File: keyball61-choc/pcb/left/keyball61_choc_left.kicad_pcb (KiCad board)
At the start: 2 copper layers, 141.9 x 107.5 mm, 141 parts, among them J1 OLED, J13 TRS_JACK, J2 Conn_01x01-Connector_Generic, J3 Conn_01x01-Connector_Generic, P1 I2C, P2 I2C, SW1 Choc_V1, SW10 Choc_V1, SW11 Choc_V1, SW12 Choc_V1, SW13 Choc_V1, SW14 Choc_V1, SW15 Choc_V1, SW16 Choc_V1, SW17 Choc_V1, SW18 Choc_V1, SW19 Choc_V1, SW2 Choc_V1, SW20 Choc_V1, SW21 Choc_V1, SW22 Choc_V1, SW23 Choc_V1, SW24 Choc_V1, SW25 Choc_V1, SW26 Choc_V1, SW27 Choc_V1, SW28 Choc_V1, SW29 Choc_V1, SW3 Choc_V1, SW30 Choc_V1, SW31 Choc_V1, SW32 Choc_V1, SW33 RESET_SW, SW4 Choc_V1, SW5 Choc_V1, SW6 Choc_V1, SW7 Choc_V1, SW8 Choc_V1, SW9 Choc_V1, U1 ProMicro-kbd

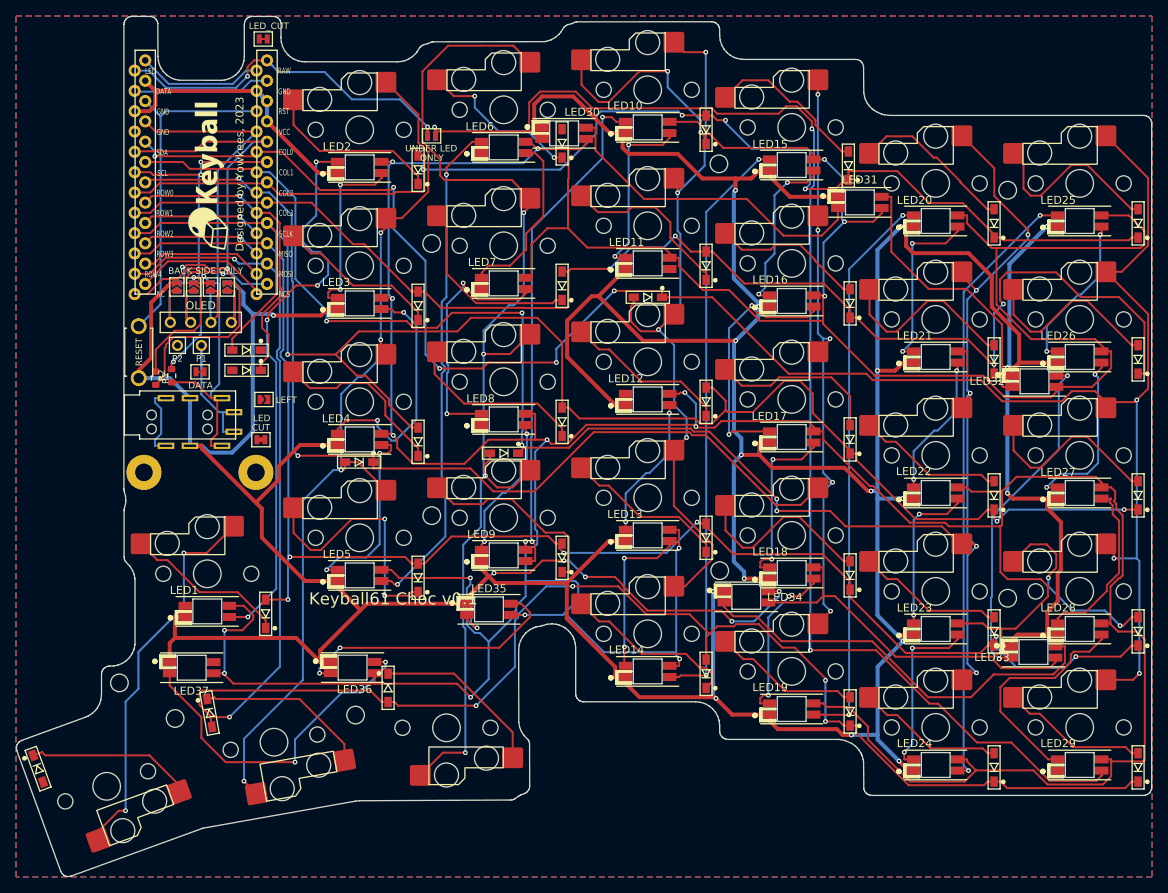
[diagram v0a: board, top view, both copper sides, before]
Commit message: WIP: routed left/right boards from previous run (DRC: L 10 err/7 open, R 9 err/11 open)
Superseded by the routing run in progress.

Co-Authored-By: Claude Opus 5.5 <noreply@anthropic.com>
Claude-Session: https://claude.ai/code/session_012Lz4SD3XgX9T3cBqnotnnt
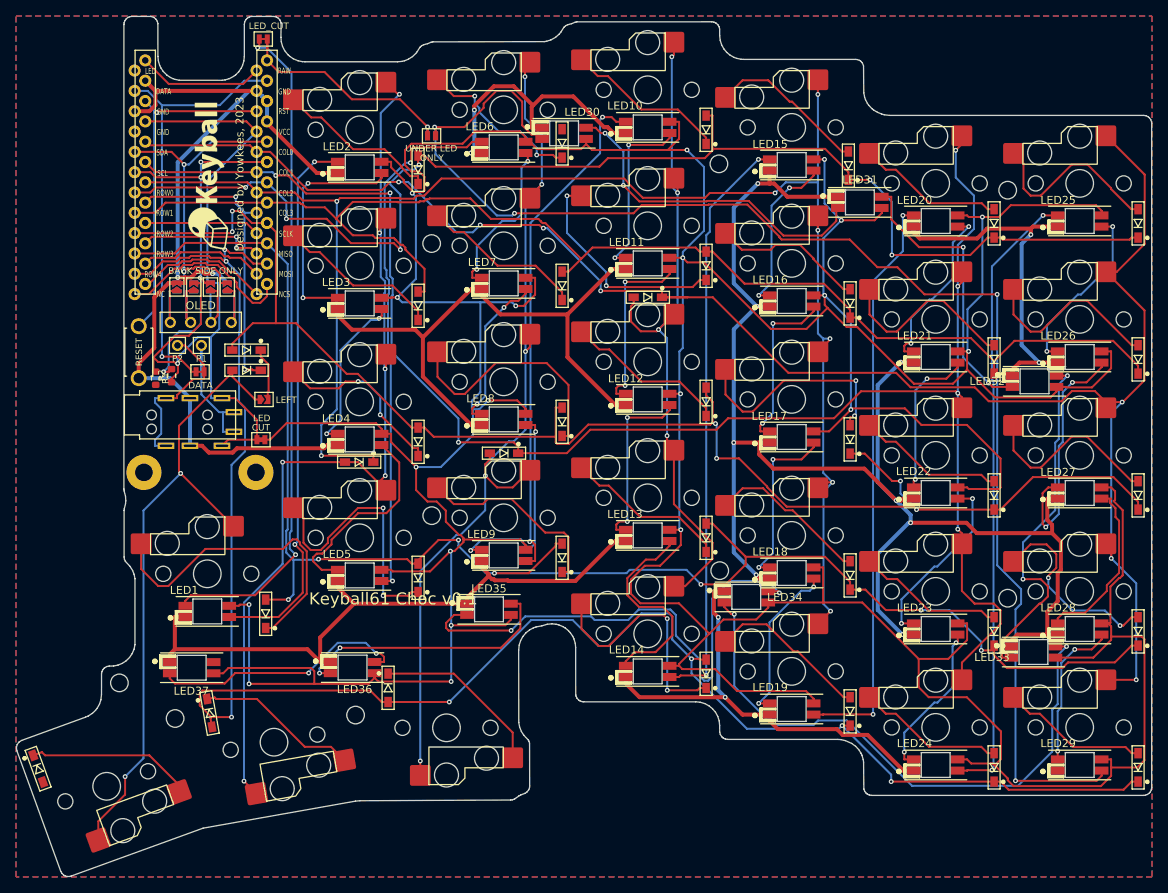
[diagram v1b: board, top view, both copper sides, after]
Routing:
- net Net-(JP12-Pad2): track 0.00 -> 84.9 mm, vias 0 -> 2
- net GND: track 659.0 -> 597.9 mm, vias 18 -> 16
- net DATA: track 17.1 -> 55.2 mm, vias 0 -> 1
- net Net-(JP11-Pad1): track 739.3 -> 706.3 mm, vias 18 -> 20
- net Net-(D37-Pad2): track 48.4 -> 80.5 mm
- net SDA: track 69.4 -> 41.4 mm, vias 2 -> 3
- net Net-(D35-Pad2): track 139.5 -> 112.5 mm, vias 4 -> 5
- net Net-(LED11-Pad2): track 0.00 -> 22.7 mm, vias 0 -> 2
- net Net-(LED33-Pad2): track 53.1 -> 73.9 mm, vias 0 -> 2
- net Net-(D26-Pad1): track 21.0 -> 40.1 mm
- net ROW2: track 206.8 -> 188.6 mm, vias 3 -> 6
- net COL0: track 245.5 -> 227.2 mm, vias 8 -> 7
- net LED: track 46.9 -> 30.3 mm, vias 2 -> 1
- net COL1: track 228.7 -> 214.1 mm, vias 10 -> 7
- net ROW3: track 190.5 -> 204.7 mm, vias 6 -> 7
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
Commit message: WIP: routed boards from previous run (DRC: L 4 err/3 open, R 10 err/8 open)
Superseded by the routing run in progress.

Co-Authored-By: Claude Opus 5.5 <noreply@anthropic.com>
Claude-Session: https://claude.ai/code/session_012Lz4SD3XgX9T3cBqnotnnt
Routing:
- net GND: track 597.9 -> 743.0 mm, vias 16 -> 10
- net Net-(JP11-Pad1): track 706.3 -> 774.6 mm, vias 20 -> 17
- net COL0: track 227.2 -> 161.1 mm, vias 7 -> 3
- net SDA: track 41.4 -> 63.4 mm, vias 3 -> 4
- net LED: track 30.3 -> 50.3 mm, vias 1 -> 2
- net Net-(LED33-Pad2): track 73.9 -> 56.1 mm, vias 2 -> 4
- net ROW2: track 188.6 -> 171.0 mm
- net Net-(LED27-Pad2): track 22.1 -> 39.4 mm
- net COL2: track 205.9 -> 222.3 mm, vias 8 -> 7
- net Net-(D26-Pad1): track 40.1 -> 26.1 mm, vias 0 -> 2
- net Net-(D25-Pad1): track 33.3 -> 20.5 mm, vias 2 -> 0
- net Net-(D4-Pad1): track 20.4 -> 30.9 mm
- net Net-(LED26-Pad2): track 31.1 -> 20.7 mm
- net Net-(D17-Pad1): track 30.3 -> 20.4 mm, vias 0 -> 2
- net Net-(LED31-Pad2): track 35.9 -> 45.5 mm
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
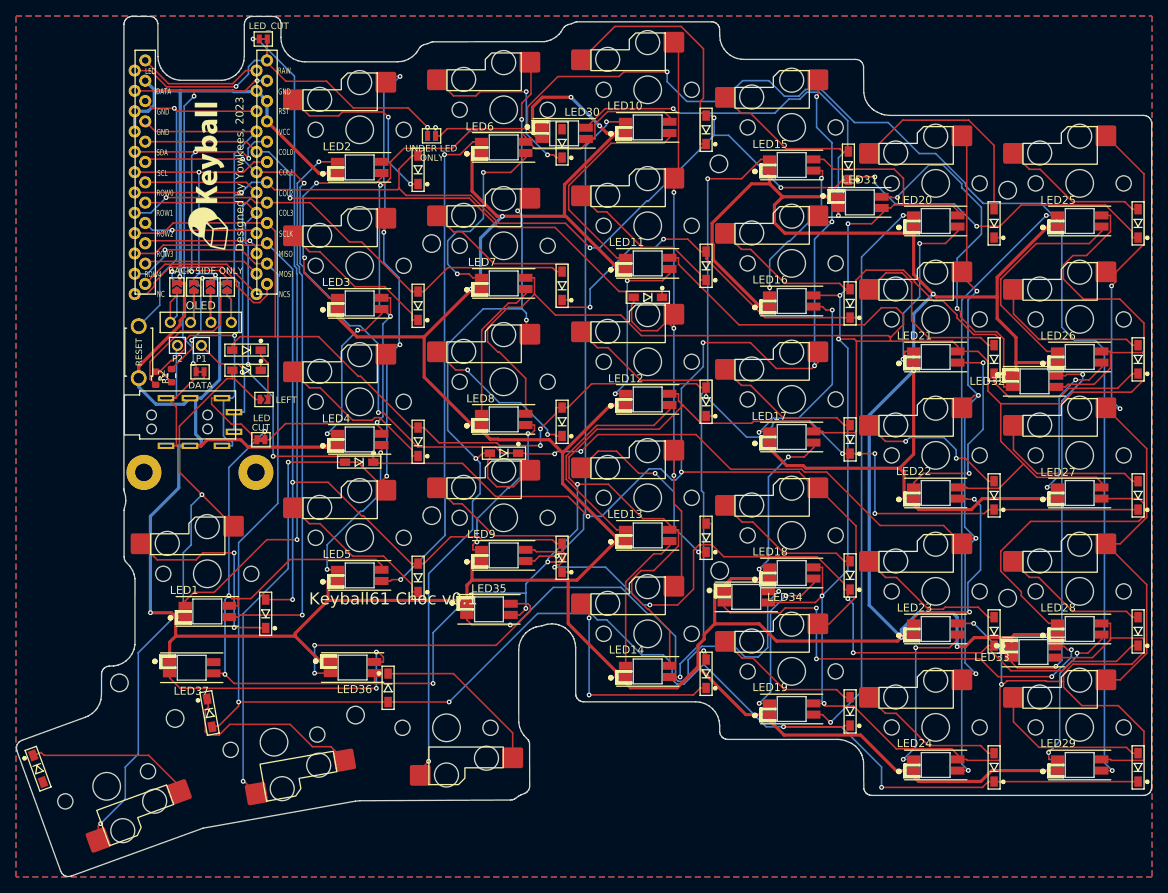
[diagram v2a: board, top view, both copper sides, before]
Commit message: WIP: boards from previous routing run (DRC: L 14 err/2 open, R 28 err/6 open)
Superseded by the iterative routing run in progress.

Co-Authored-By: Claude Opus 5.5 <noreply@anthropic.com>
Claude-Session: https://claude.ai/code/session_012Lz4SD3XgX9T3cBqnotnnt
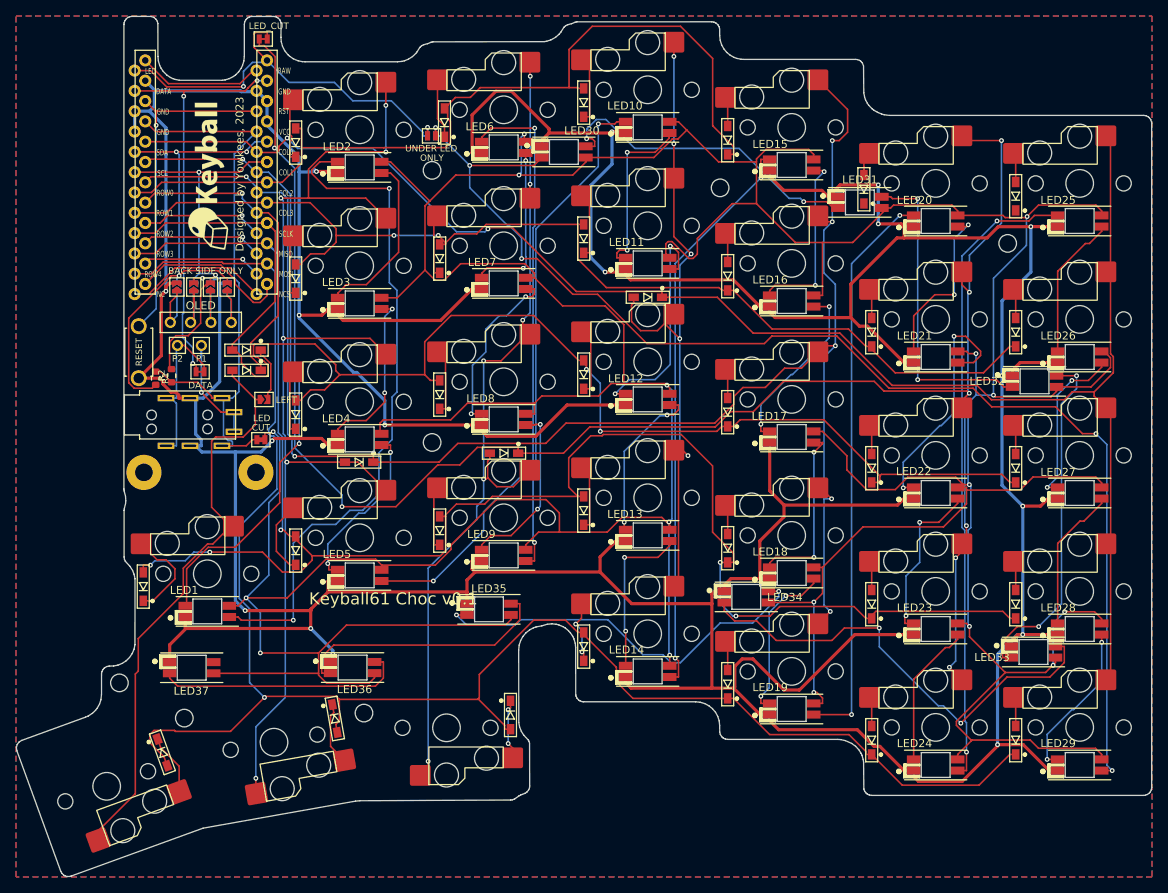
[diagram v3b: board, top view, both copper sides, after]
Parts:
- removed MH5, MH7: M2, keyball61_choc:MountingHole_2.2mm_M2
- moved D2 16.8 mm to (186.1, 64.1)
- moved D27 15.7 mm to (205.1, 133.0)
- moved D28 15.7 mm to (187.1, 133.0)
- moved D20 15.7 mm to (205.1, 116.0)
- moved D21 15.7 mm to (187.1, 116.0)
- moved D22 15.7 mm to (169.1, 109.0)
- moved D23 15.7 mm to (151.1, 104.3)
- moved D24 15.7 mm to (133.1, 106.8)
- moved D30 15.7 mm to (151.1, 121.3)
- moved D31 15.7 mm to (142.0, 129.8)
- moved D4 15.7 mm to (151.1, 53.3)
- moved D1 15.7 mm to (205.1, 65.0)
- moved D10 15.7 mm to (151.1, 70.3)
- moved D11 15.7 mm to (133.1, 72.8)
- moved D13 15.7 mm to (205.1, 99.0)
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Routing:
- net Net-(JP11-Pad1): track 774.6 -> 688.2 mm
- net ROW0: track 156.4 -> 109.0 mm, vias 6 -> 0
- net COL0: track 161.1 -> 206.9 mm, vias 3 -> 2
- net ROW1: track 165.0 -> 135.0 mm, vias 3 -> 2
- net Net-(D36-Pad2): track 118.2 -> 141.0 mm
- net Net-(D4-Pad1): track 30.9 -> 8.27 mm
- net Net-(D2-Pad2): track 26.6 -> 4.01 mm
- net Net-(LED27-Pad2): track 39.4 -> 18.2 mm
- net Net-(D8-Pad2): track 23.0 -> 3.69 mm
- net Net-(D30-Pad1): track 26.8 -> 7.84 mm
- net Net-(D13-Pad2): track 20.3 -> 3.69 mm
- net Net-(D7-Pad2): track 20.3 -> 3.69 mm
- net Net-(D27-Pad2): track 20.3 -> 3.69 mm
- net COL2: track 222.3 -> 206.3 mm
- net Net-(D23-Pad1): track 24.2 -> 8.27 mm, vias 2 -> 0
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
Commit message: Iteratively routed boards (0 DRC violations; L 2 / R 7 open) + fixup.py grid router with rip-up
Co-Authored-By: Claude Opus 5.5 <noreply@anthropic.com>
Claude-Session: https://claude.ai/code/session_012Lz4SD3XgX9T3cBqnotnnt
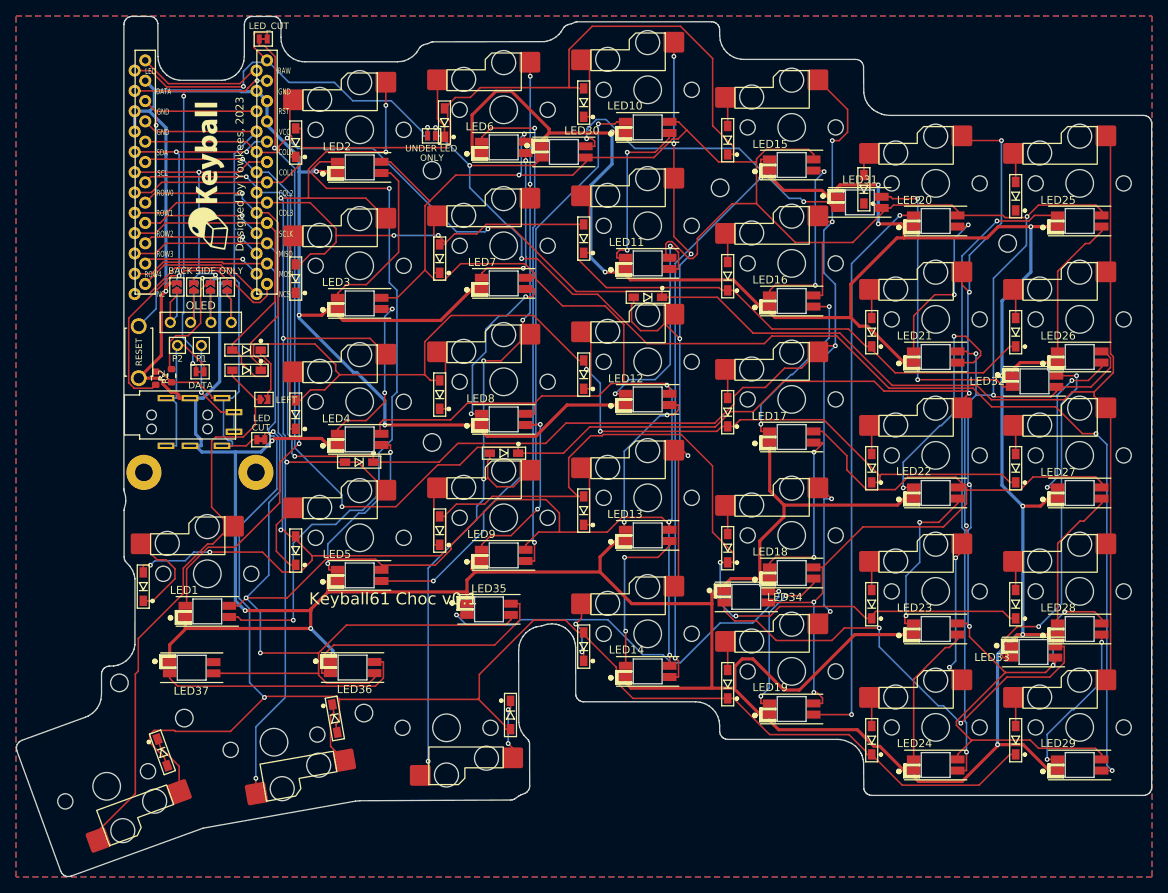
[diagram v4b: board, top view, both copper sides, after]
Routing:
- net Net-(J1-Pad2): track 10.0 -> 8.24 mm
- net Net-(J13-PadA): track 14.8 -> 13.4 mm
- net GND: track 745.7 -> 744.7 mm
- net Net-(D2-Pad2): track 4.01 -> 3.00 mm
- net ROW3: track 211.5 -> 210.5 mm
- net LED: track 54.0 -> 53.2 mm
- net ROW2: track 175.4 -> 174.7 mm
- net Net-(U1-Pad12): track 22.5 -> 21.8 mm
- net ROW4: track 219.5 -> 219.0 mm
- net Net-(D32-Pad1): track 8.41 -> 7.87 mm
- net Net-(JP12-Pad2): track 81.8 -> 81.3 mm
- net Net-(JP13-Pad1): track 158.2 -> 157.7 mm
- net Net-(LED33-Pad2): track 58.8 -> 58.3 mm
- net Net-(J13-PadB): track 21.2 -> 20.7 mm

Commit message: Keyball61 Choc v0.1: DRC-clean routed PCBs, JLC fab files, bottom plates, renders
Both halves: 0 DRC errors, 0 unconnected (KiCad 9). Gerbers + drill,
JLC BOM/CPL (single-sided assembly), 2 mm acrylic bottom plates with the
original trackball-case holes, and 3D renders. Docs updated.

Co-Authored-By: Claude Opus 5.5 <noreply@anthropic.com>
Claude-Session: https://claude.ai/code/session_012Lz4SD3XgX9T3cBqnotnnt
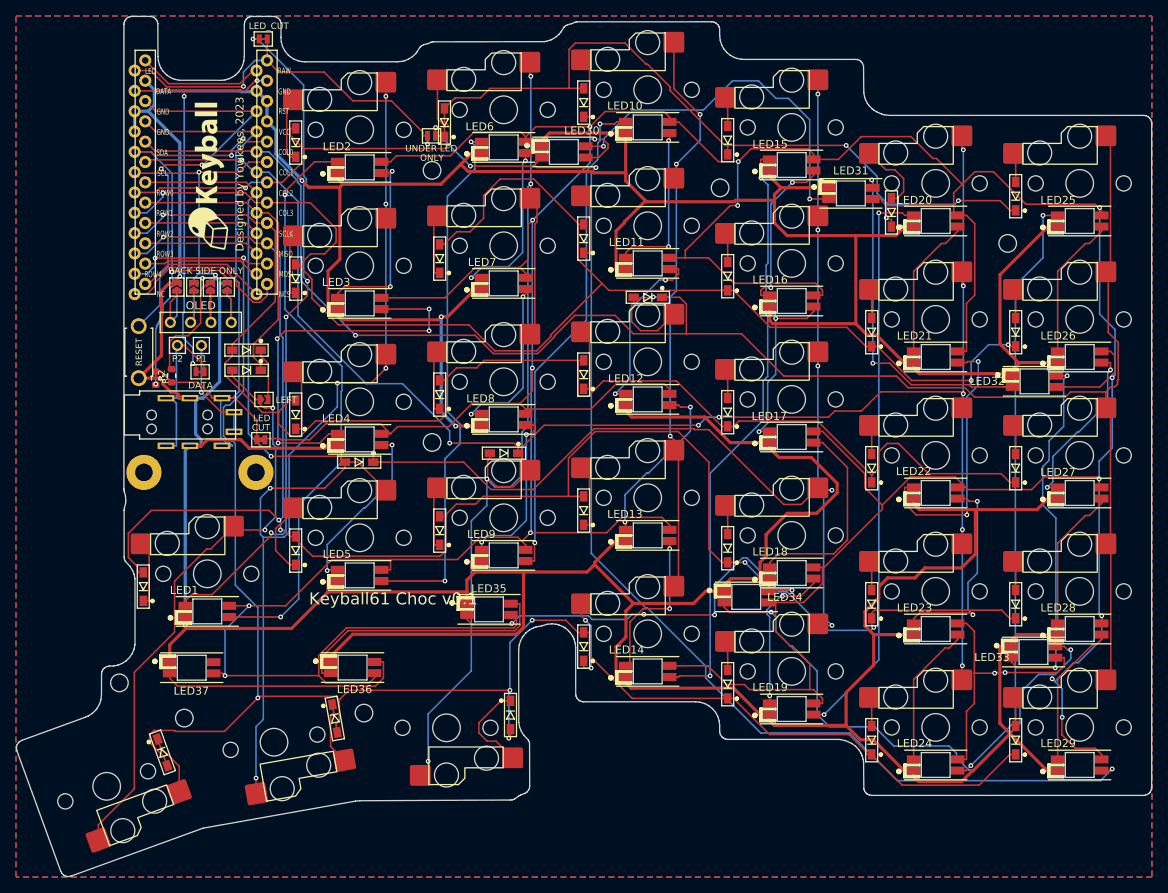
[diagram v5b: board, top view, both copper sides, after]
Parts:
- moved D2 4.50 mm to (189.6, 67.0)
- moved LED31 1.59 mm to (184.5, 64.6)
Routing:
- net ROW1: track 135.0 -> 178.2 mm, vias 2 -> 3
- net ROW0: track 109.0 -> 146.1 mm, vias 0 -> 4
- net Net-(LED3-Pad2): track 21.2 -> 49.1 mm, vias 2 -> 4
- net COL1: track 229.8 -> 203.8 mm, vias 8 -> 9
- net Net-(D35-Pad2): track 109.3 -> 127.6 mm, vias 6 -> 4
- net COL0: track 206.5 -> 223.0 mm, vias 2 -> 1
- net Net-(D36-Pad2): track 141.0 -> 127.6 mm
- net Net-(LED1-Pad2): track 85.2 -> 73.9 mm
- net Net-(LED33-Pad2): track 58.3 -> 68.2 mm
- net Net-(LED5-Pad2): track 76.1 -> 67.2 mm
- net RESET: track 42.2 -> 50.9 mm, vias 1 -> 2
- net Net-(LED11-Pad2): track 29.0 -> 22.2 mm
- net Net-(D2-Pad2): track 3.00 -> 9.08 mm
- net Net-(LED30-Pad2): track 40.5 -> 46.2 mm
- net Net-(LED22-Pad2): track 20.8 -> 25.9 mm
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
